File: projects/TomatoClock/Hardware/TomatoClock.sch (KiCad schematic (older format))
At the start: 18 parts, among them J1 ICSP, J2 UART, J3 Screen, J4 Ultrasonic, J5 CC2541_Bluetooth, Q1 9014, U1 ATmega328P-PU, Y1 16MHz

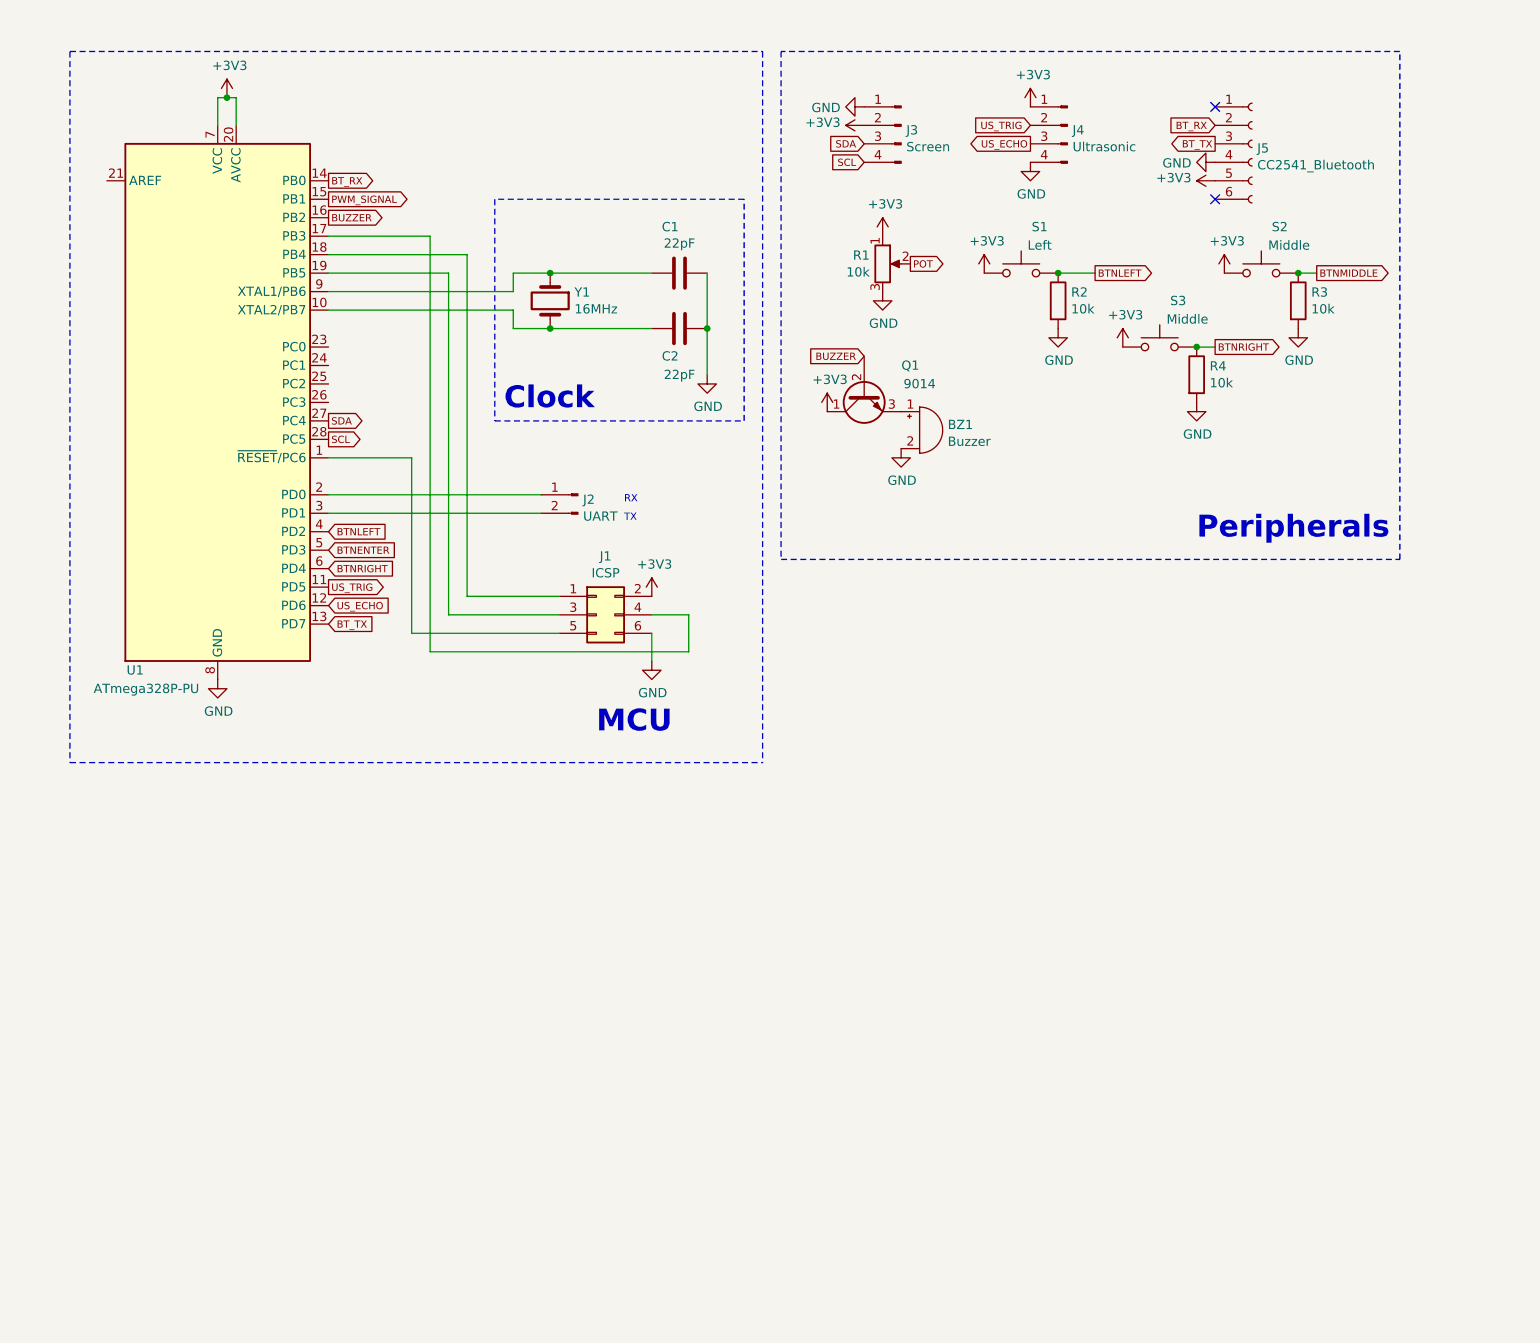
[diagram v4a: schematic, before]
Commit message: TomatoClock: Change U1 from ATmega328p to STM32F103C8T6; Add power management citcuit; Update PCB
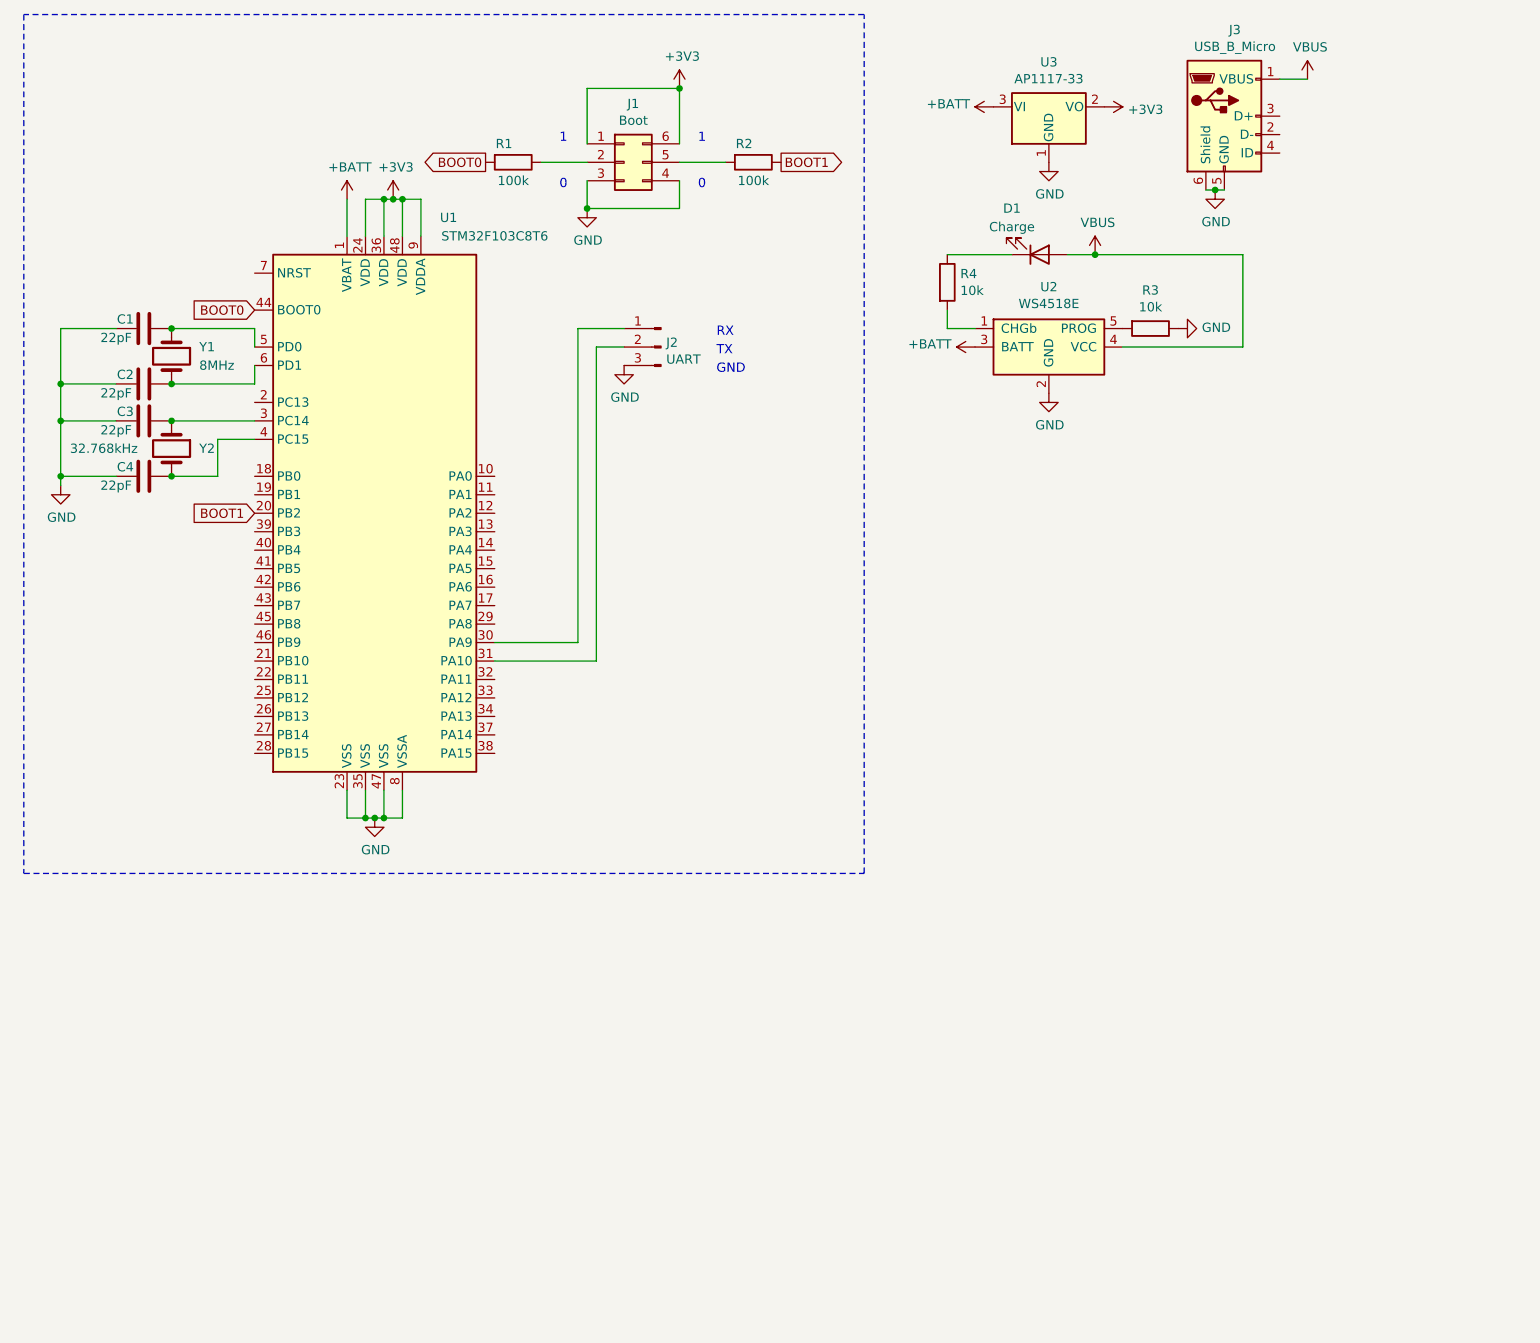
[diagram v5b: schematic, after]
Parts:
- removed BZ1: Buzzer, symbol Device:Buzzer
- removed J1: ICSP, Connector_PinHeader_2.00mm:PinHeader_2x03_P2.00mm_Vertical, symbol Connector_Generic:Conn_02x03_Odd_Even
- removed J2: UART, symbol Connector:Conn_01x02_Male
- removed J3: Screen, Connector_PinHeader_2.00mm:PinHeader_1x04_P2.00mm_Vertical, symbol Connector:Conn_01x04_Male
- removed J4: Ultrasonic, Connector_PinHeader_2.00mm:PinHeader_1x04_P2.00mm_Vertical, symbol Connector:Conn_01x04_Male
- removed J5: CC2541_Bluetooth, symbol Connector:Conn_01x06_Female
- removed Q1: 9014, Package_TO_SOT_THT:TO-92_HandSolder, symbol Device:Q_NPN_CBE
- removed R1: 10k, symbol Device:R_POT
- removed S1: Left, Button_Switch_THT:SW_PUSH_6mm_H4.3mm, symbol Switch:SW_Push
- removed S2, S3: Middle, Button_Switch_THT:SW_PUSH_6mm_H4.3mm, symbol Switch:SW_Push
- removed U1: ATmega328P-PU, Package_DIP:DIP-28_W7.62mm, symbol MCU_Microchip_ATmega:ATmega328P-PU
- added C3, C4: 22pF, Capacitor_THT:C_Disc_D3.0mm_W1.6mm_P2.50mm, symbol Device:C
- added D1: Charge, LED_THT:LED_D3.0mm, symbol Device:LED
- added J1: Boot, Connector_PinHeader_2.00mm:PinHeader_2x03_P2.00mm_Vertical, symbol Connector_Generic:Conn_02x03_Counter_Clockwise
- added J2: UART, Connector_PinHeader_2.00mm:PinHeader_1x03_P2.00mm_Vertical, symbol Connector:Conn_01x03_Male
- added J3: USB_B_Micro, Connector_USB:USB_Micro-B_Molex-105017-0001, symbol Connector:USB_B_Micro
- added R1: 100k, Resistor_THT:R_Axial_DIN0204_L3.6mm_D1.6mm_P5.08mm_Horizontal, symbol Device:R
- added U1: STM32F103C8T6, Package_QFP:LQFP-48_7x7mm_P0.5mm, symbol MCU_ST_STM32F1:STM32F103C8Tx
- added U2: WS4518E, Package_TO_SOT_SMD:SOT-23-5_HandSoldering, symbol Power_Management:WS4518E
- added U3: AP1117-33, Package_TO_SOT_SMD:SOT-223-3_TabPin2, symbol Regulator_Linear:AP1117-33
- added Y2: 32.768kHz, Crystal:Crystal_DS26_D2.0mm_L6.0mm_Horizontal_1EP_style1, symbol Device:Crystal
- R2: value 10k -> 100k; footprint (none) -> Resistor_THT:R_Axial_DIN0204_L3.6mm_D1.6mm_P5.08mm_Horizontal
- R3, R4: footprint (none) -> Resistor_THT:R_Axial_DIN0204_L3.6mm_D1.6mm_P5.08mm_Horizontal
- Y1: value 16MHz -> 8MHz
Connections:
- net BTNMIDDLE is gone; now on net GND: R3.1
- net +3V3: now also J1.1 (Pin_1), J1.6 (Pin_6), U1.24 (VDD), U1.36 (VDD), U1.48 (VDD), U1.9 (VDDA), U3.2 (VO)
- net GND: now also C1.2, C3.2, C4.2, J1.3 (Pin_3), J1.4 (Pin_4), J2.3 (Pin_3), J3.5 (GND), J3.6 (Shield), U1.23 (VSS), U1.35 (VSS), U1.47 (VSS), U1.8 (VSSA), U2.2 (GND), U3.1 (GND); no longer C1.1, R2.2, R3.2, R4.2
- net at C2.1, Y1.2: now also U1.6 (PD1)
- net at Y1.1: now also C1.1, U1.5 (PD0); no longer C1.2
- net BTNLEFT renamed BOOT1
- net BOOT1: now also U1.20 (PB2)
- net BTNRIGHT: no longer names the net of R4.1
- net BTNRIGHT: now also D1.1 (K)
- new net: C3.1, U1.3 (PC14), Y2.1
- new net: J2.1 (Pin_1), U1.30 (PA9)
- new net: J2.2 (Pin_2), U1.31 (PA10)
- new net: C4.1, U1.4 (PC15), Y2.2
- new net: J1.2 (Pin_2), R1.1
- new net: J1.5 (Pin_5), R2.2
- new net: R4.2, U2.1 (CHGb)
- new net: R3.2, U2.5 (PROG)
- new net +BATT: U1.1 (VBAT), U2.3 (BATT), U3.3 (VI)
- new net BOOT0: R1.2, U1.44 (BOOT0)
- new net VBUS: D1.2 (A), J3.1 (VBUS), U2.4 (VCC)
- no-connect marks 2 -> 0
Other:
- note added: "0"
- note added: "1"
- note added: "GND"
- note removed: "Clock"
- note removed: "MCU"
- note removed: "Peripherals"

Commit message: TomatoClock: Update PCB and Gerber files
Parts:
- removed J1: Boot, Connector_PinHeader_2.00mm:PinHeader_2x03_P2.00mm_Vertical, symbol Connector_Generic:Conn_02x03_Counter_Clockwise
- added BZ1: Buzzer, Buzzer_Beeper:Buzzer_15x7.5RM7.6, symbol Device:Buzzer
- added H1, H2, H3, H4: hole, MountingHole:MountingHole_2.2mm_M2, symbol Mechanical:MountingHole_Pad
- added J1: Boot, Connector_PinHeader_2.00mm:PinHeader_2x03_P2.00mm_Vertical, symbol Connector_Generic:Conn_02x03_Odd_Even
- added J4: Ultrasonic, Connector_PinSocket_2.00mm:PinSocket_1x04_P2.00mm_Vertical, symbol Connector:Conn_01x04_Male
- added J5: Buttons, Connector_PinHeader_2.00mm:PinHeader_1x05_P2.00mm_Vertical, symbol Connector:Conn_01x05_Male
- added J6: Battery, Connector_Molex:Molex_Micro-Latch_53253-0270_1x02_P2.00mm_Vertical, symbol Connector:Conn_01x02_Male
- added Q1: S9014, Package_TO_SOT_THT:TO-92, symbol Device:Q_NPN_CBE
- R1, R2, R3, R4: footprint Resistor_THT:R_Axial_DIN0204_L3.6mm_D1.6mm_P5.08mm_Horizontal -> Resistor_SMD:R_0603_1608Metric
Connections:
- net +3V3: now also J1.1 (Pin_1), J1.2 (Pin_2), J4.1 (Pin_1), J5.1 (Pin_1), Q1.1 (C)
- net +BATT: now also J6.2 (Pin_2)
- net GND: now also BZ1.2 (+), H1.1, H2.1, H3.1, H4.1, J1.5 (Pin_5), J1.6 (Pin_6), J4.4 (Pin_4), J5.5 (Pin_5), J6.1 (Pin_1)
- net BT_RXD: now reaches U1.12 (PA2)
- net BT_TXD: now reaches U1.13 (PA3)
- net LEFT: now reaches U1.14 (PA4)
- net LEFT: now also J5.2 (Pin_2)
- net MIDDLE: now reaches U1.15 (PA5)
- net MIDDLE: now also J5.3 (Pin_3)
- net RIGHT: now reaches U1.16 (PA6)
- net RIGHT: now also J5.4 (Pin_4)
- net US_TRIG: now reaches U1.17 (PA7)
- net US_TRIG: now also J4.2 (Pin_2)
- net US_ECHO: now reaches U1.18 (PB0)
- net US_ECHO: now also J4.3 (Pin_3)
- net BUZZER: now reaches U1.19 (PB1)
- net BUZZER: now also Q1.2 (B)
- net SCL: now reaches U1.45 (PB8)
- net SDA: now reaches U1.46 (PB9)
- net at R1.1: now also J1.3 (Pin_3)
- net at R2.2: now also J1.4 (Pin_4)
- new net: BZ1.1 (-), Q1.3 (E)

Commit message: TomatoClock: Update C1-C4 from TH to SMD
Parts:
- C1, C2, C3, C4: footprint Capacitor_THT:C_Disc_D3.0mm_W1.6mm_P2.50mm -> Capacitor_SMD:C_0603_1608Metric
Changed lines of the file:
@@
 F 0 "C1" V 1150 2150 50  0000 C CNN
 F 1 "22pF" V 1250 2100 50  0000 C CNN
-F 2 "Capacitor_THT:C_Disc_D3.0mm_W1.6mm_P2.50mm" H 1238 2100 50  0001 C CNN
+F 2 "Capacitor_SMD:C_0603_1608Metric" H 1238 2100 50  0001 C CNN
 F 3 "~" H 1200 2250 50  0001 C CNN
 	1    1200 2250
@@
 F 0 "C2" V 1150 2450 50  0000 C CNN
 F 1 "22pF" V 1250 2400 50  0000 C CNN
-F 2 "Capacitor_THT:C_Disc_D3.0mm_W1.6mm_P2.50mm" H 1238 2400 50  0001 C CNN
+F 2 "Capacitor_SMD:C_0603_1608Metric" H 1238 2400 50  0001 C CNN
 F 3 "~" H 1200 2550 50  0001 C CNN
 	1    1200 2550
@@
 F 0 "C3" V 1150 2650 50  0000 C CNN
 F 1 "22pF" V 1250 2600 50  0000 C CNN
-F 2 "Capacitor_THT:C_Disc_D3.0mm_W1.6mm_P2.50mm" H 1238 2600 50  0001 C CNN
+F 2 "Capacitor_SMD:C_0603_1608Metric" H 1238 2600 50  0001 C CNN
 F 3 "~" H 1200 2750 50  0001 C CNN
 	1    1200 2750
@@
 F 0 "C4" V 1150 2950 50  0000 C CNN
 F 1 "22pF" V 1250 2900 50  0000 C CNN
-F 2 "Capacitor_THT:C_Disc_D3.0mm_W1.6mm_P2.50mm" H 1238 2900 50  0001 C CNN
+F 2 "Capacitor_SMD:C_0603_1608Metric" H 1238 2900 50  0001 C CNN
 F 3 "~" H 1200 3050 50  0001 C CNN
 	1    1200 3050
